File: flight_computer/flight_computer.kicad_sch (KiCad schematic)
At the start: 0 parts

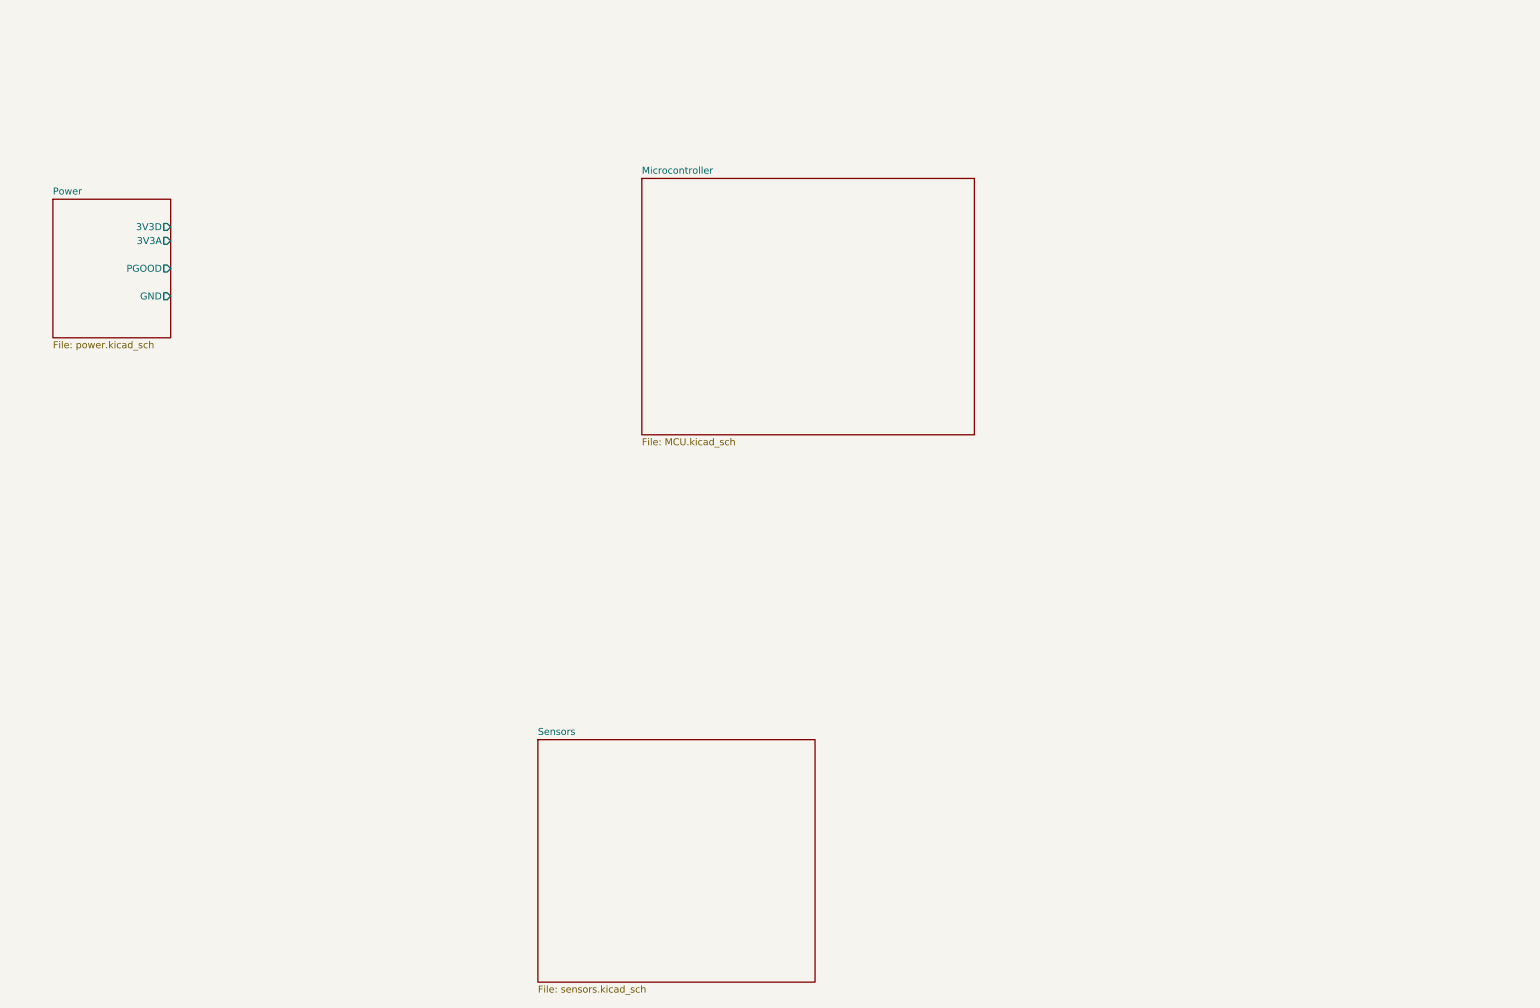
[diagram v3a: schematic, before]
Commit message: Tidying up schematics and adding most missing sections (Not finished GPS)
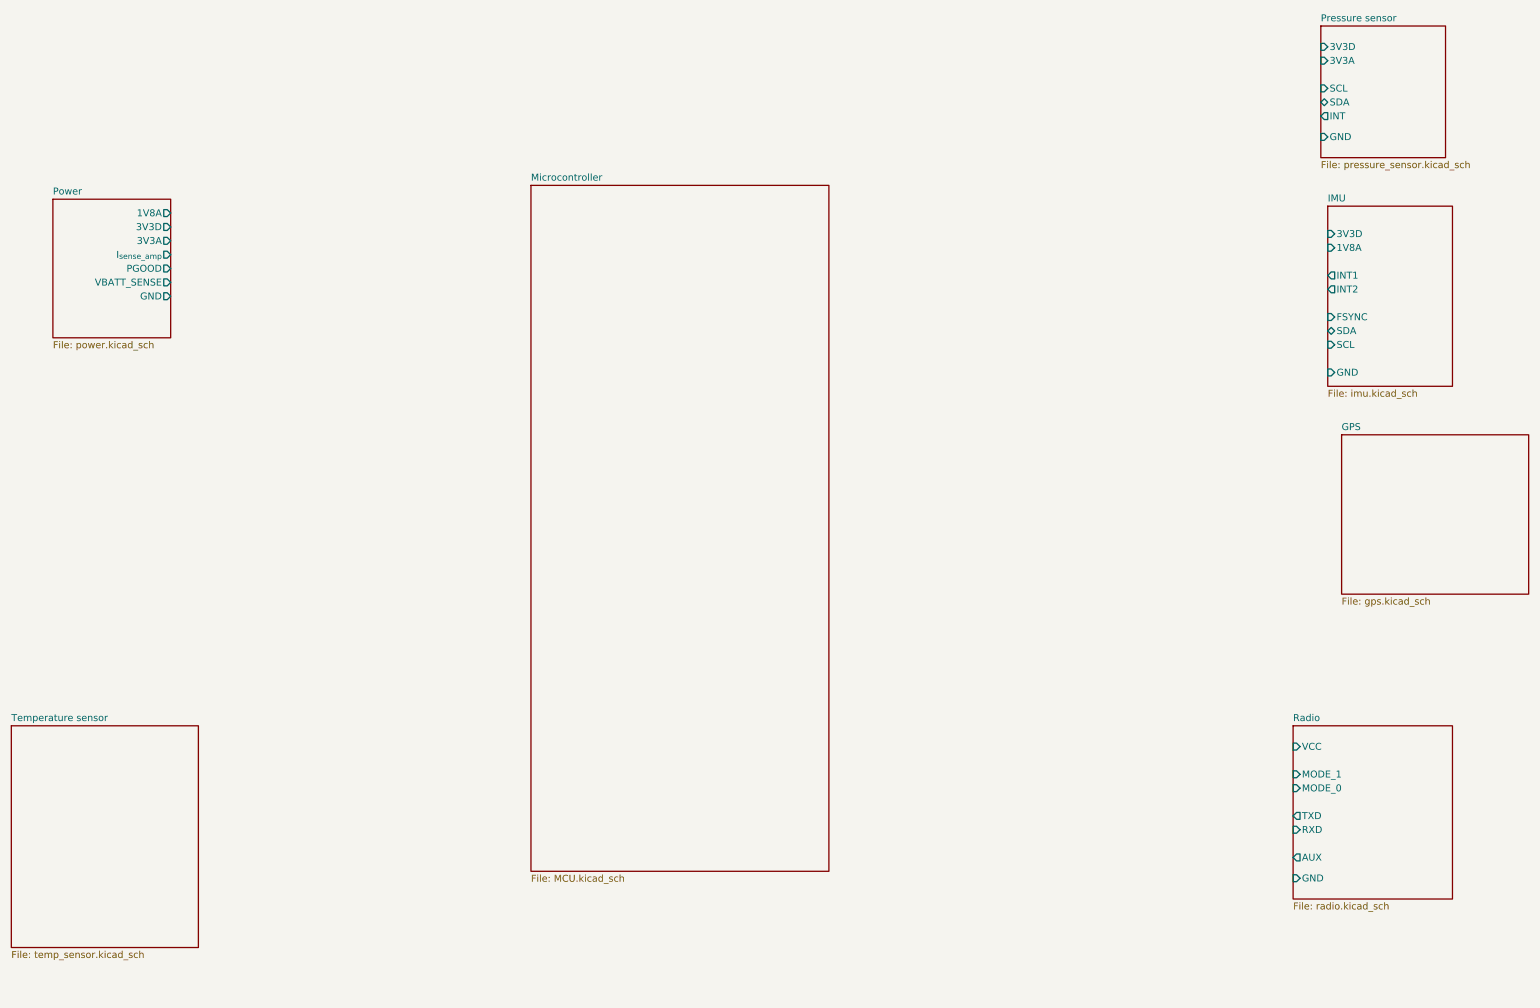
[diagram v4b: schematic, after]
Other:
- sheet Sensors renamed Pressure sensor
- added sheet GPS (gps.kicad_sch)
- added sheet IMU (imu.kicad_sch)
- added sheet Radio (radio.kicad_sch)
- added sheet Temperature sensor (temp_sensor.kicad_sch)
- sheet Power ports: added 1V8A, I_{sense_amp}, VBATT_SENSE; removed none
- sheet Pressure sensor: file sensors.kicad_sch -> pressure_sensor.kicad_sch
- sheet Pressure sensor ports: added 3V3A, 3V3D, GND, INT, SCL, SDA; removed none
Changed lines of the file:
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@@
 (kicad_sch (version 20230121) (generator eeschema)
   (paper "A3")
-  (sheet (at 179.07 54.61) (size 60.96 46.99) (fields_autoplaced)
+  (sheet (at 304.8 59.69) (size 22.86 33.02) (fields_autoplaced)
     (stroke (width 0.1524) (type solid))
     (fill (color 0 0 0 0.0000))
-    (property "Sheetname" "Microcontroller" (at 179.07 53.8984 0)
+    (property "Sheetname" "IMU" (at 304.8 58.9784 0)
       (effects (font (size 1.27 1.27)) (justify left bottom))
     )
-    (property "Sheetfile" "MCU.kicad_sch" (at 179.07 102.1846 0)
+    (property "Sheetfile" "imu.kicad_sch" (at 304.8 93.2946 0)
+      (effects (font (size 1.27 1.27)) (justify left top))
+    )
+    (pin "INT2" output (at 304.8 74.93 180)
+      (effects (font (size 1.27 1.27)) (justify left))
+    )
+    (pin "INT1" output (at 304.8 72.39 180)
+      (effects (font (size 1.27 1.27)) (justify left))
+    )
+    (pin "1V8A" input (at 304.8 67.31 180)
+      (effects (font (size 1.27 1.27)) (justify left))
+    )
+    (pin "3V3D" input (at 304.8 64.77 180)
+      (effects (font (size 1.27 1.27)) (justify left))
+    )
+    (pin "GND" input (at 304.8 90.17 180)
+      (effects (font (size 1.27 1.27)) (justify left))
+    )
+    (pin "SCL" input (at 304.8 85.09 180)
+      (effects (font (size 1.27 1.27)) (justify left))
+    )
+    (pin "SDA" bidirectional (at 304.8 82.55 180)
+      (effects (font (size 1.27 1.27)) (justify left))
+    )
+    (pin "FSYNC" input (at 304.8 80.01 180)
+      (effects (font (size 1.27 1.27)) (justify left))
+    )
+    (instances
+      (project "flight_computer"
+        (path "/89a81c02-14e9-456f-a334-ff69a24bd093" (page "7"))
+      )
+    )
+  )
+  (sheet (at 298.45 154.94) (size 29.21 31.75) (fields_autoplaced)
+    (stroke (width 0.1524) (type solid))
+    (fill (color 0 0 0 0.0000))
+    (property "Sheetname" "Radio" (at 298.45 154.2284 0)
+      (effects (font (size 1.27 1.27)) (justify left bottom))
+    )
+    (property "Sheetfile" "radio.kicad_sch" (at 298.45 187.2746 0)
+      (effects (font (size 1.27 1.27)) (justify left top))
+    )
+    (pin "AUX" output (at 298.45 179.07 180)
+      (effects (font (size 1.27 1.27)) (justify left))
+    )
+    (pin "GND" input (at 298.45 182.88 180)
+      (effects (font (size 1.27 1.27)) (justify left))
+    )
+    (pin "VCC" input (at 298.45 158.75 180)
+      (effects (font (size 1.27 1.27)) (justify left))
+    )
+    (pin "RXD" input (at 298.45 173.99 180)
+      (effects (font (size 1.27 1.27)) (justify left))
+    )
+    (pin "MODE_1" input (at 298.45 163.83 180)
+      (effects (font (size 1.27 1.27)) (justify left))
+    )
+    (pin "TXD" output (at 298.45 171.45 180)
+      (effects (font (size 1.27 1.27)) (justify left))
+    )
+    (pin "MODE_0" input (at 298.45 166.37 180)
+      (effects (font (size 1.27 1.27)) (justify left))
+    )
+    (instances
+      (project "flight_computer"
+        (path "/89a81c02-14e9-456f-a334-ff69a24bd093" (page "6"))
+      )
+    )
+  )
+  (sheet (at 158.75 55.88) (size 54.61 125.73) (fields_autoplaced)
+    (stroke (width 0.1524) (type solid))
+    (fill (color 0 0 0 0.0000))
+    (property "Sheetname" "Microcontroller" (at 158.75 55.1684 0)
+      (effects (font (size 1.27 1.27)) (justify left bottom))
+    )
+    (property "Sheetfile" "MCU.kicad_sch" (at 158.75 182.1946 0)
       (effects (font (size 1.27 1.27)) (justify left top))
     )
@@
     )
   )
-  (sheet (at 160.02 157.48) (size 50.8 44.45) (fields_autoplaced)
+  (sheet (at 63.5 154.94) (size 34.29 40.64) (fields_autoplaced)
     (stroke (width 0.1524) (type solid))
     (fill (color 0 0 0 0.0000))
-    (property "Sheetname" "Sensors" (at 160.02 156.7684 0)
+    (property "Sheetname" "Temperature sensor" (at 63.5 154.2284 0)
       (effects (font (size 1.27 1.27)) (justify left bottom))
     )
-    (property "Sheetfile" "sensors.kicad_sch" (at 160.02 202.5146 0)
+    (property "Sheetfile" "temp_sensor.kicad_sch" (at 63.5 196.1646 0)
       (effects (font (size 1.27 1.27)) (justify left top))
+    )
+    (instances
+      (project "flight_computer"
+        (path "/89a81c02-14e9-456f-a334-ff69a24bd093" (page "8"))
+      )
+    )
+  )
+  (sheet (at 307.34 101.6) (size 34.29 29.21) (fields_autoplaced)
+    (stroke (width 0.1524) (type solid))
+    (fill (color 0 0 0 0.0000))
+    (property "Sheetname" "GPS" (at 307.34 100.8884 0)
+      (effects (font (size 1.27 1.27)) (justify left bottom))
+    )
+    (property "Sheetfile" "gps.kicad_sch" (at 307.34 131.3946 0)
+      (effects (font (size 1.27 1.27)) (justify left top))
+    )
+    (instances
+      (project "flight_computer"
+        (path "/89a81c02-14e9-456f-a334-ff69a24bd093" (page "5"))
+      )
+    )
+  )
+  (sheet (at 303.53 26.67) (size 22.86 24.13) (fields_autoplaced)
+    (stroke (width 0.1524) (type solid))
+    (fill (color 0 0 0 0.0000))
+    (property "Sheetname" "Pressure sensor" (at 303.53 25.9584 0)
+      (effects (font (size 1.27 1.27)) (justify left bottom))
+    )
+    (property "Sheetfile" "pressure_sensor.kicad_sch" (at 303.53 51.3846 0)
+      (effects (font (size 1.27 1.27)) (justify left top))
+    )
+    (pin "3V3A" input (at 303.53 33.02 180)
+      (effects (font (size 1.27 1.27)) (justify left))
+    )
+    (pin "GND" input (at 303.53 46.99 180)
+      (effects (font (size 1.27 1.27)) (justify left))
+    )
+    (pin "INT" output (at 303.53 43.18 180)
+      (effects (font (size 1.27 1.27)) (justify left))
+    )
+    (pin "SCL" input (at 303.53 38.1 180)
+      (effects (font (size 1.27 1.27)) (justify left))
+    )
+    (pin "SDA" bidirectional (at 303.53 40.64 180)
+      (effects (font (size 1.27 1.27)) (justify left))
+    )
+    (pin "3V3D" input (at 303.53 30.48 180)
+      (effects (font (size 1.27 1.27)) (justify left))
     )
     (instances
@@
       (effects (font (size 1.27 1.27)) (justify right))
     )
+    (pin "VBATT_SENSE" output (at 92.71 73.66 0)
+      (effects (font (size 1.27 1.27)) (justify right))
+    )
+    (pin "I_{sense_amp}" output (at 92.71 68.58 0)
+      (effects (font (size 1.27 1.27)) (justify right))
+    )
+    (pin "1V8A" output (at 92.71 60.96 0)
+      (effects (font (size 1.27 1.27)) (justify right))
+    )

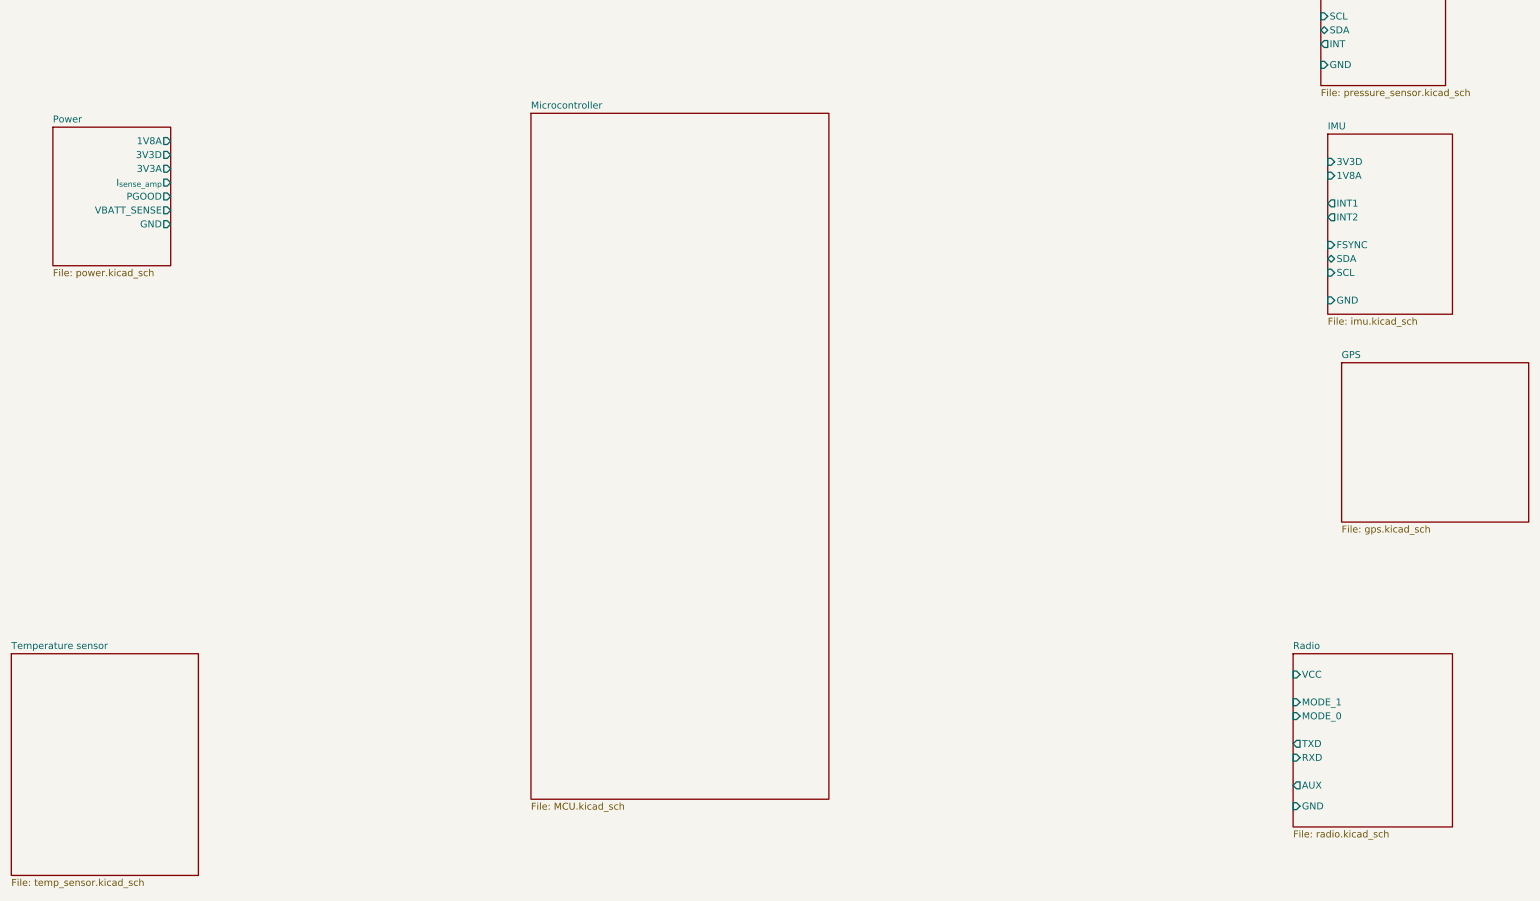
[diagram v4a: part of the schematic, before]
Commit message: Finishing gps, ready to connect all
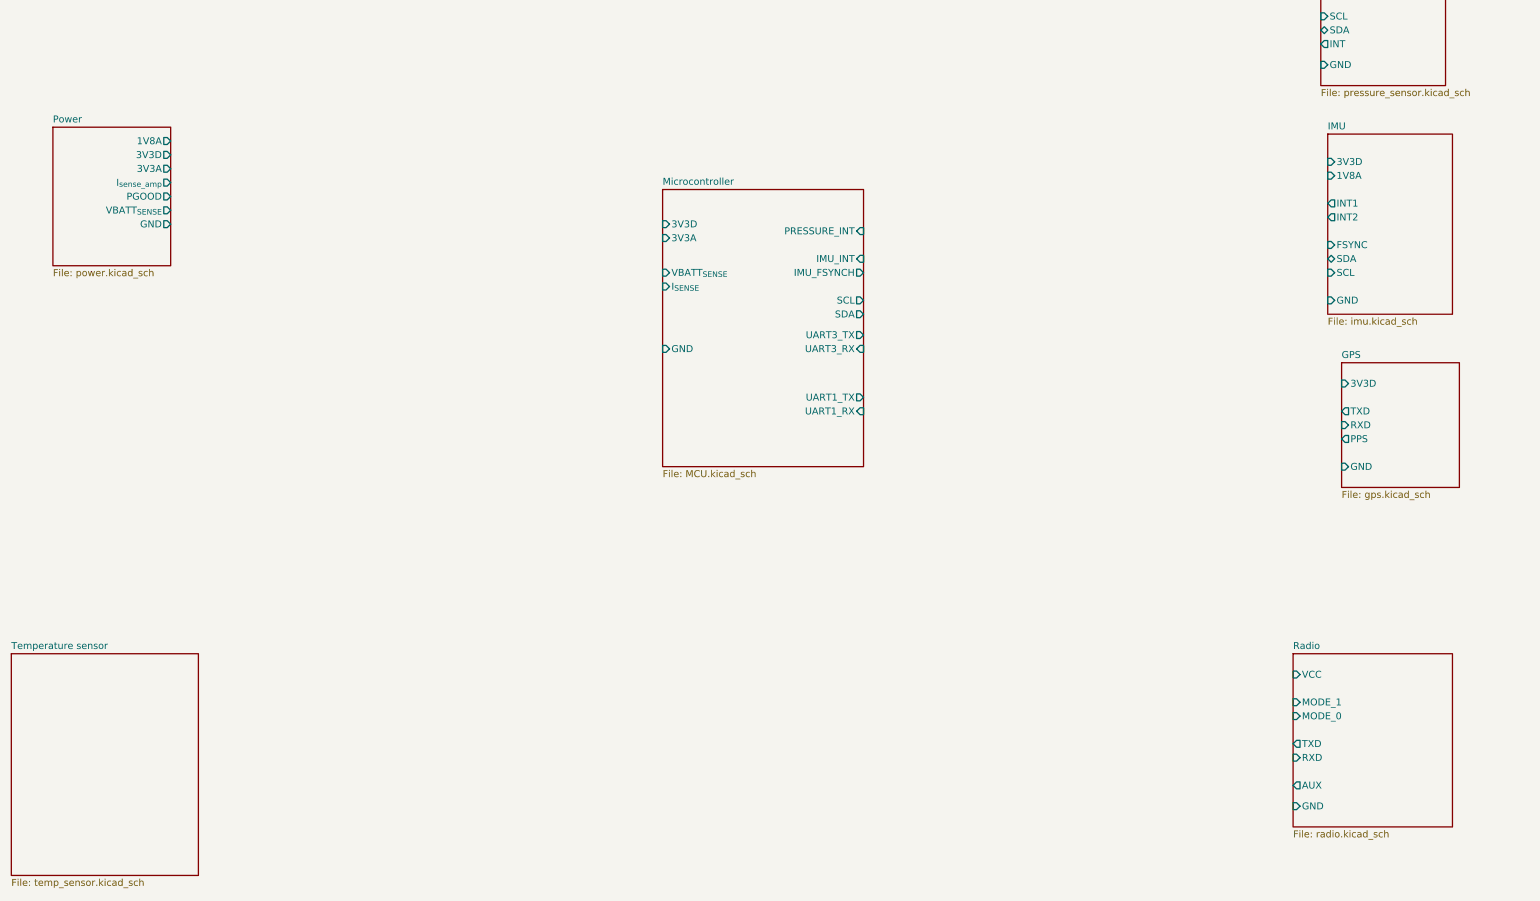
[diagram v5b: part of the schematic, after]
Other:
- sheet GPS ports: added 3V3D, GND, PPS, RXD, TXD; removed none
- sheet Microcontroller ports: added 3V3A, 3V3D, GND, IMU_FSYNCH, IMU_INT, I_{SENSE}, PRESSURE_INT, SCL, SDA, UART1_RX, UART1_TX, UART3_RX, UART3_TX, VBATT_{SENSE}; removed none
- sheet Power ports: added VBATT_{SENSE}; removed VBATT_SENSE
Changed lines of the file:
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@@
     )
   )
-  (sheet (at 158.75 55.88) (size 54.61 125.73) (fields_autoplaced)
+  (sheet (at 182.88 69.85) (size 36.83 50.8) (fields_autoplaced)
     (stroke (width 0.1524) (type solid))
     (fill (color 0 0 0 0.0000))
-    (property "Sheetname" "Microcontroller" (at 158.75 55.1684 0)
+    (property "Sheetname" "Microcontroller" (at 182.88 69.1384 0)
       (effects (font (size 1.27 1.27)) (justify left bottom))
     )
-    (property "Sheetfile" "MCU.kicad_sch" (at 158.75 182.1946 0)
+    (property "Sheetfile" "MCU.kicad_sch" (at 182.88 121.2346 0)
       (effects (font (size 1.27 1.27)) (justify left top))
+    )
+    (pin "UART3_RX" input (at 219.71 99.06 0)
+      (effects (font (size 1.27 1.27)) (justify right))
+    )
+    (pin "UART3_TX" output (at 219.71 96.52 0)
+      (effects (font (size 1.27 1.27)) (justify right))
+    )
+    (pin "VBATT_{SENSE}" input (at 182.88 85.09 180)
+      (effects (font (size 1.27 1.27)) (justify left))
+    )
+    (pin "UART1_RX" input (at 219.71 110.49 0)
+      (effects (font (size 1.27 1.27)) (justify right))
+    )
+    (pin "UART1_TX" output (at 219.71 107.95 0)
+      (effects (font (size 1.27 1.27)) (justify right))
+    )
+    (pin "SCL" output (at 219.71 90.17 0)
+      (effects (font (size 1.27 1.27)) (justify right))
+    )
+    (pin "SDA" output (at 219.71 92.71 0)
+      (effects (font (size 1.27 1.27)) (justify right))
+    )
+    (pin "I_{SENSE}" input (at 182.88 87.63 180)
+      (effects (font (size 1.27 1.27)) (justify left))
+    )
+    (pin "IMU_INT" input (at 219.71 82.55 0)
+      (effects (font (size 1.27 1.27)) (justify right))
+    )
+    (pin "PRESSURE_INT" input (at 219.71 77.47 0)
+      (effects (font (size 1.27 1.27)) (justify right))
+    )
+    (pin "IMU_FSYNCH" output (at 219.71 85.09 0)
+      (effects (font (size 1.27 1.27)) (justify right))
+    )
+    (pin "3V3D" input (at 182.88 76.2 180)
+      (effects (font (size 1.27 1.27)) (justify left))
+    )
+    (pin "GND" input (at 182.88 99.06 180)
+      (effects (font (size 1.27 1.27)) (justify left))
+    )
+    (pin "3V3A" input (at 182.88 78.74 180)
+      (effects (font (size 1.27 1.27)) (justify left))
     )
     (instances
@@
     )
   )
-  (sheet (at 307.34 101.6) (size 34.29 29.21) (fields_autoplaced)
+  (sheet (at 307.34 101.6) (size 21.59 22.86) (fields_autoplaced)
     (stroke (width 0.1524) (type solid))
     (fill (color 0 0 0 0.0000))
@@
       (effects (font (size 1.27 1.27)) (justify left bottom))
     )
-    (property "Sheetfile" "gps.kicad_sch" (at 307.34 131.3946 0)
+    (property "Sheetfile" "gps.kicad_sch" (at 307.34 125.0446 0)
       (effects (font (size 1.27 1.27)) (justify left top))
+    )
+    (pin "PPS" output (at 307.34 115.57 180)
+      (effects (font (size 1.27 1.27)) (justify left))
+    )
+    (pin "GND" input (at 307.34 120.65 180)
+      (effects (font (size 1.27 1.27)) (justify left))
+    )
+    (pin "3V3D" input (at 307.34 105.41 180)
+      (effects (font (size 1.27 1.27)) (justify left))
+    )
+    (pin "TXD" output (at 307.34 110.49 180)
+      (effects (font (size 1.27 1.27)) (justify left))
+    )
+    (pin "RXD" input (at 307.34 113.03 180)
+      (effects (font (size 1.27 1.27)) (justify left))
     )
     (instances
@@
       (effects (font (size 1.27 1.27)) (justify right))
     )
-    (pin "VBATT_SENSE" output (at 92.71 73.66 0)
-      (effects (font (size 1.27 1.27)) (justify right))
-    )
     (pin "I_{sense_amp}" output (at 92.71 68.58 0)
       (effects (font (size 1.27 1.27)) (justify right))
@@
       (effects (font (size 1.27 1.27)) (justify right))
     )
+    (pin "VBATT_{SENSE}" output (at 92.71 73.66 0)
+      (effects (font (size 1.27 1.27)) (justify right))
+    )
